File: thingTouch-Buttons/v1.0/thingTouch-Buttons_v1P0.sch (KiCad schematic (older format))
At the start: 0 parts

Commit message: intermediate commit
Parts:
- added C? (x3): 30pF, symbol C_Small
- added W? (x3): touchPad, symbol touchPad
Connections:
- new net: C?.1, W?.1 (OUT) (x3)
- new net GND: C?.2, C?.2, C?.2
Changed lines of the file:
@@
 LIBS:contrib
 LIBS:valves
-LIBS:esp-32_wroom32_rectangle
-LIBS:AMS1117-3V3
-LIBS:usb_a_4_pins
-LIBS:cp2102
-LIBS:JTAG
-LIBS:crystal-new
-LIBS:usb_a_male_pcb
+LIBS:touchpad_single
+LIBS:thingTouch-Buttons_v1P0-cache
 EELAYER 25 0
 EELAYER END
@@
 Sheet 1 1
 Title ""
-Date ""
+Date "2017-07-17"
 Rev ""
 Comp ""
@@
 Comment4 ""
 $EndDescr
+$Comp
+L touchPad W?
+U 1 1 596CD996
+P 2250 2475
+F 0 "W?" H 2250 2675 60  0000 C CNN
+F 1 "touchPad" H 2250 2275 60  0000 C CNN
+F 2 "" H 2250 2475 60  0001 C CNN
+F 3 "" H 2250 2475 60  0001 C CNN
+	1    2250 2475
+	1    0    0    -1
+$EndComp
+$Comp
+L touchPad W?
+U 1 1 596CD9C3
+P 2250 3075
+F 0 "W?" H 2250 3275 60  0000 C CNN
+F 1 "touchPad" H 2250 2875 60  0000 C CNN
+F 2 "" H 2250 3075 60  0001 C CNN
+F 3 "" H 2250 3075 60  0001 C CNN
+	1    2250 3075
+	1    0    0    -1
+$EndComp
+$Comp
+L touchPad W?
+U 1 1 596CDA11
+P 2250 3750
+F 0 "W?" H 2250 3950 60  0000 C CNN
+F 1 "touchPad" H 2250 3550 60  0000 C CNN
+F 2 "" H 2250 3750 60  0001 C CNN
+F 3 "" H 2250 3750 60  0001 C CNN
+	1    2250 3750
+	1    0    0    -1
+$EndComp
+$Comp
+L C_Small C?
+U 1 1 596CDAC2
+P 3150 2600
+F 0 "C?" H 3160 2670 50  0000 L CNN
+F 1 "30pF" H 3160 2520 50  0000 L CNN
+F 2 "" H 3150 2600 50  0000 C CNN
+F 3 "" H 3150 2600 50  0000 C CNN
+	1    3150 2600
+	1    0    0    -1
+$EndComp
+$Comp
+L GND #PWR?
+U 1 1 596CDD3A
+P 2900 4125
+F 0 "#PWR?" H 2900 4175 30  0001 C CNN
+F 1 "GND" H 2900 4000 30  0001 C CNN
+F 2 "" H 2900 4125 60  0000 C CNN
+F 3 "" H 2900 4125 60  0000 C CNN
+	1    2900 4125
+	1    0    0    -1
+$EndComp
+Wire Wire Line
+	3150 2500 3150 2475
+Wire Wire Line
+	3150 2475 2600 2475
+Wire Wire Line
+	2600 3075 3150 3075
+Wire Wire Line
+	3150 3075 3150 3100
+Wire Wire Line
+	2600 3750 3150 3750
+Wire Wire Line
+	3150 3750 3150 3775
+Wire Wire Line
+	2900 2700 2900 4125
+Wire Wire Line
+	2900 3975 3150 3975
+Wire Wire Line
+	2900 3300 3150 3300
+Connection ~ 2900 3975
+Wire Wire Line
+	2900 2700 3150 2700
+Connection ~ 2900 3300
+$Comp
+L C_Small C?
+U 1 1 596CE5E0
+P 3150 3200
+F 0 "C?" H 3160 3270 50  0000 L CNN
+F 1 "30pF" H 3160 3120 50  0000 L CNN
+F 2 "" H 3150 3200 50  0000 C CNN
+F 3 "" H 3150 3200 50  0000 C CNN
+	1    3150 3200
+	1    0    0    -1
+$EndComp
+$Comp
+L C_Small C?
+U 1 1 596CE611
+P 3150 3875
+F 0 "C?" H 3160 3945 50  0000 L CNN
+F 1 "30pF" H 3160 3795 50  0000 L CNN
+F 2 "" H 3150 3875 50  0000 C CNN
+F 3 "" H 3150 3875 50  0000 C CNN
+	1    3150 3875
+	1    0    0    -1
+$EndComp
 $EndSCHEMATC

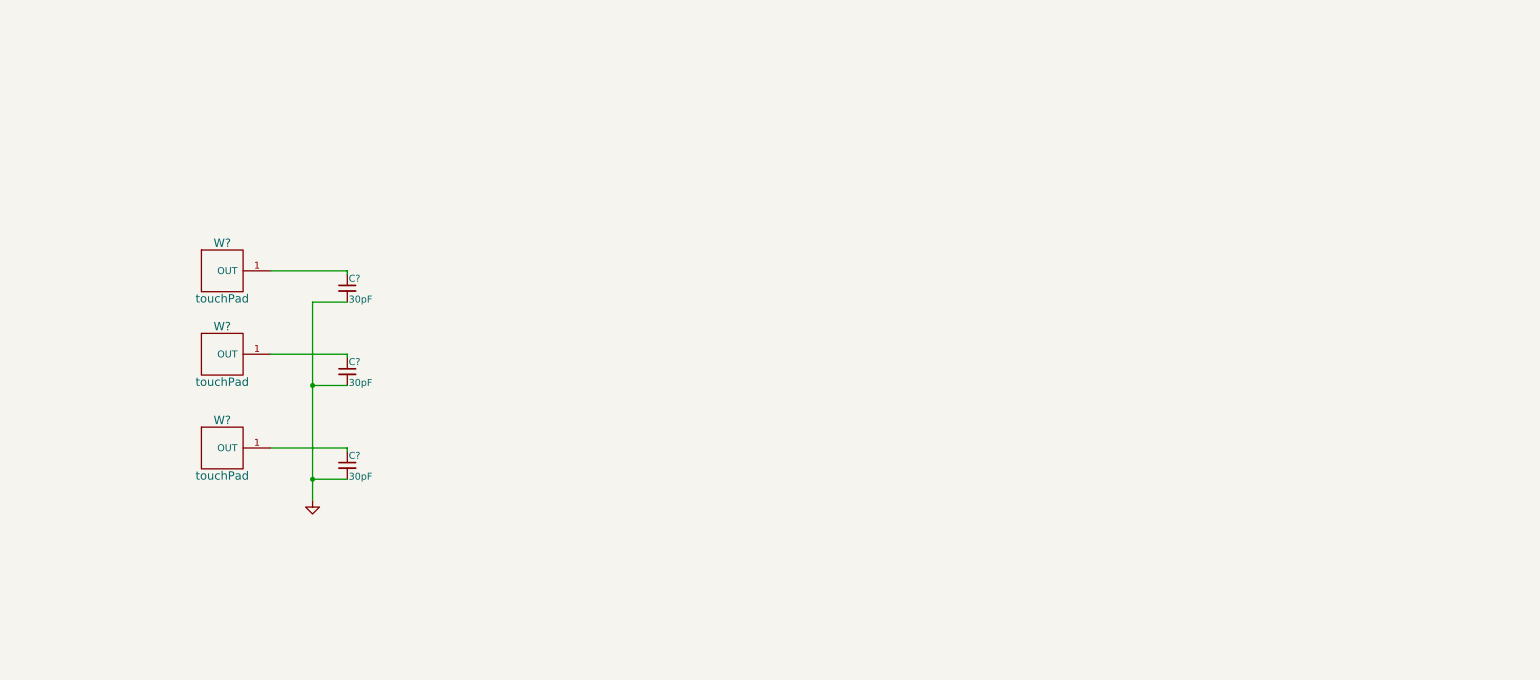
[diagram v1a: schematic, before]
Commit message: schematic complete with 3 buttons
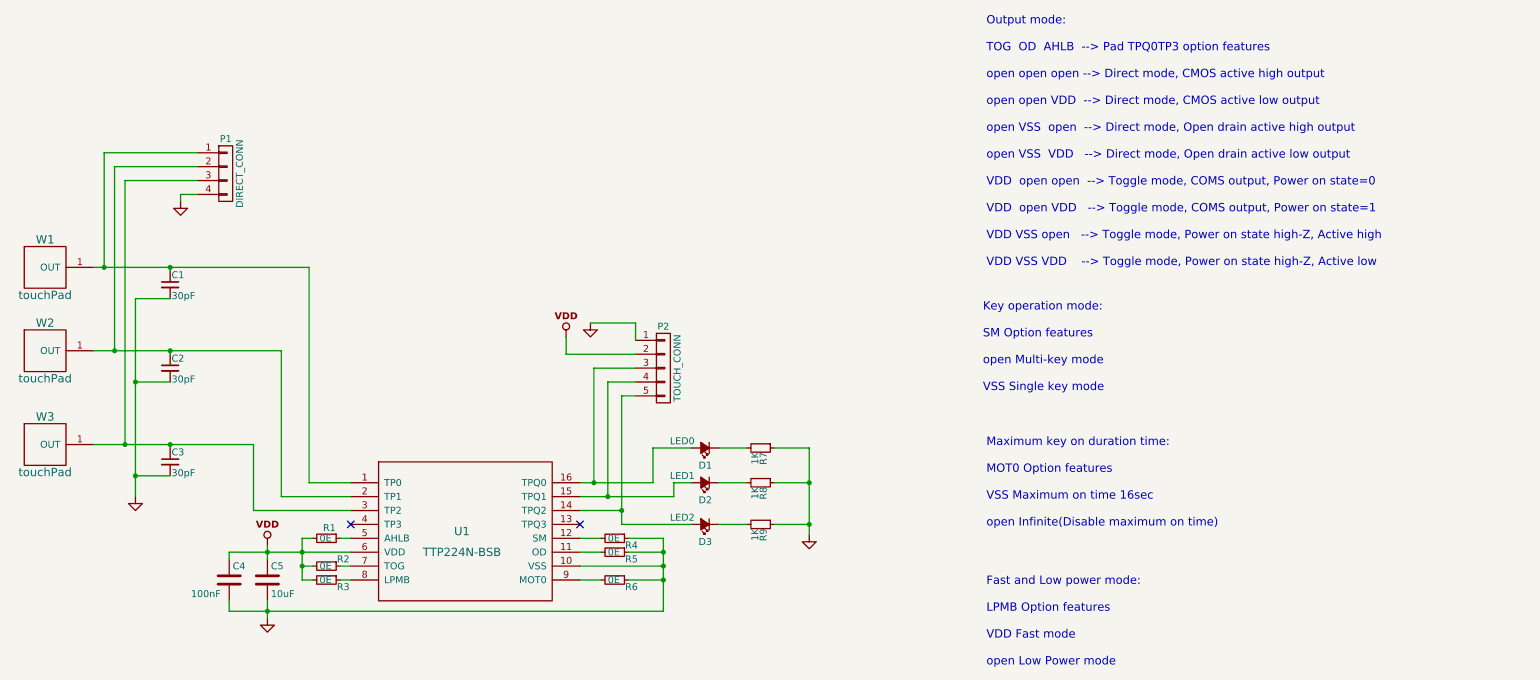
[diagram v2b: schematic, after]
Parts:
- added C4: 100nF, symbol C
- added C5: 10uF, symbol C
- added D1: LED0, symbol Led_Small
- added D2: LED1, symbol Led_Small
- added D3: LED2, symbol Led_Small
- added P1: DIRECT_CONN, symbol CONN_01X04
- added P2: TOUCH_CONN, symbol CONN_01X05
- added R1, R2, R3, R4, R5, R6: 0E, symbol R_Small
- added R7, R8, R9: 1K, symbol R_Small
- added U1: TTP224N-BSB, symbol TTP224N-BSB
- gave numbers to parts that had none: 6
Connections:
- net GND: now also C4.2, C5.2, P1.4 (P4), P2.1 (P1), R4.1, R5.1, R6.1, R7.1, R8.1, R9.1, U1.10 (VSS)
- net at C1.1, W1.1 (OUT): now also P1.1 (P1), U1.1 (TP0)
- net at C2.1, W2.1 (OUT): now also P1.2 (P2), U1.2 (TP1)
- net at C3.1, W3.1 (OUT): now also P1.3 (P3), U1.3 (TP2)
- new net: R5.2, U1.11 (OD)
- new net: R4.2, U1.12 (SM)
- new net: D3.2 (A), P2.5 (P5), U1.14 (TPQ2)
- new net: D2.2 (A), P2.4 (P4), U1.15 (TPQ1)
- new net: D1.2 (A), P2.3 (P3), U1.16 (TPQ0)
- new net: R1.1, U1.5 (AHLB)
- new net: R2.1, U1.7 (TOG)
- new net: R3.1, U1.8 (LPMB)
- new net: R6.2, U1.9 (MOT0)
- new net: D2.1 (K), R8.2
- new net: D1.1 (K), R7.2
- new net: D3.1 (K), R9.2
- new net VDD: C4.1, C5.1, P2.2 (P2), R1.2, R2.2, R3.2, U1.6 (VDD)
- no-connect marks 0 -> 2
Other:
- note added: "Fast and Low power mode:\n\nLPMB Option features\n\nVDD Fast mode\n\nopen Low Power mode"
- note added: "Key operation mode:\n\nSM Option features\n\nopen Multi-key mode\n\nVSS Single key mode"
- note added: "Maximum key on duration time:\n\nMOT0 Option features\n\nVSS Maximum on time 16sec\n\nopen Infinite(Disable maximum on time)"
- note added: "Output mode:\n\nTOG OD AHLB --> Pad TPQ0TP3 option features\n\nopen open open --> Direct mode, CMOS active high output\n\nopen open VDD --> Direct mode, CMOS active low output\n\nopen VSS open --> Direct mode, Open drain active high output\n\nopen VSS VDD --> Direct mode, Open drain active low output\n\nVDD open open --> Toggle mode, COMS output, Power on state=0\n\nVDD open VDD --> Toggle mode, 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"
- moved on the sheet: C1, C2, C3, W1, W2, W3
